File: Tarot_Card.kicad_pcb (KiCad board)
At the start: 2 copper layers, 87 x 64.2 mm, 13 parts, among them U2 ESP32-PICO-D4

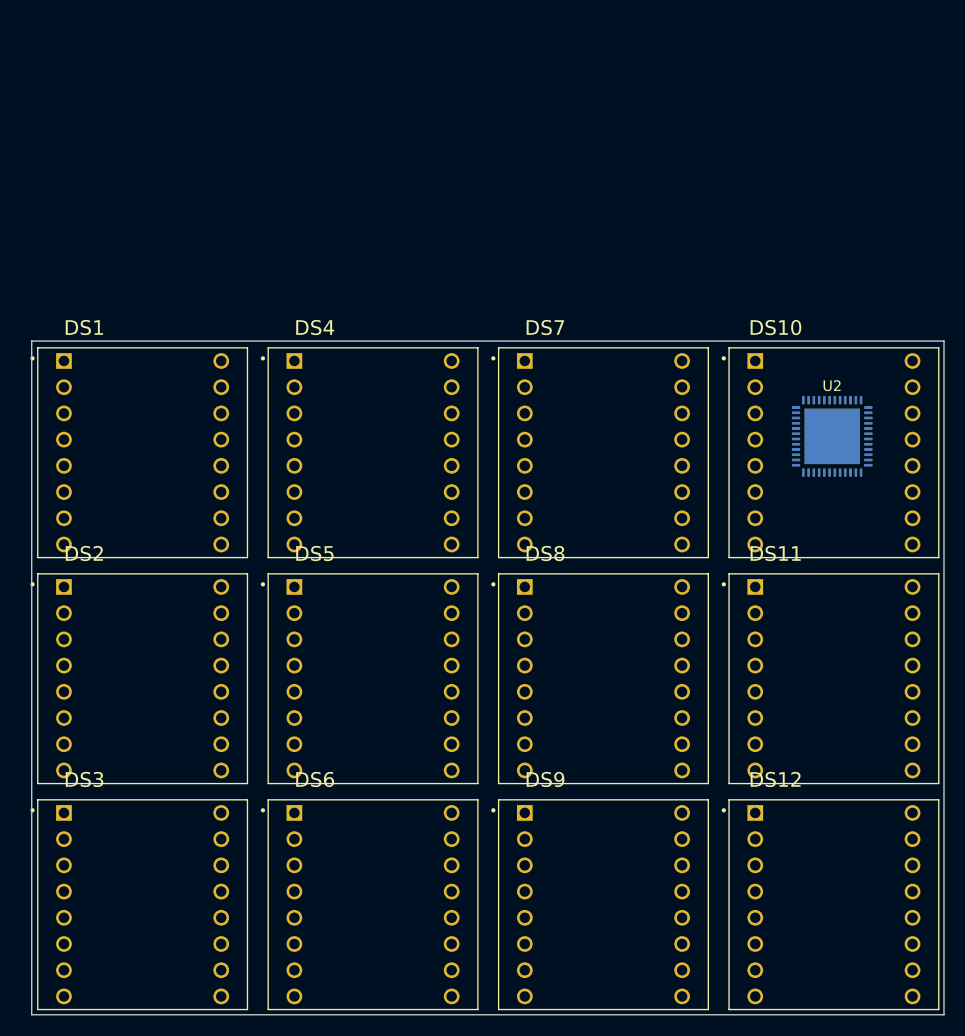
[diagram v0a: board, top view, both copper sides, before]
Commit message: Remove obsolete auto-saved files and backups
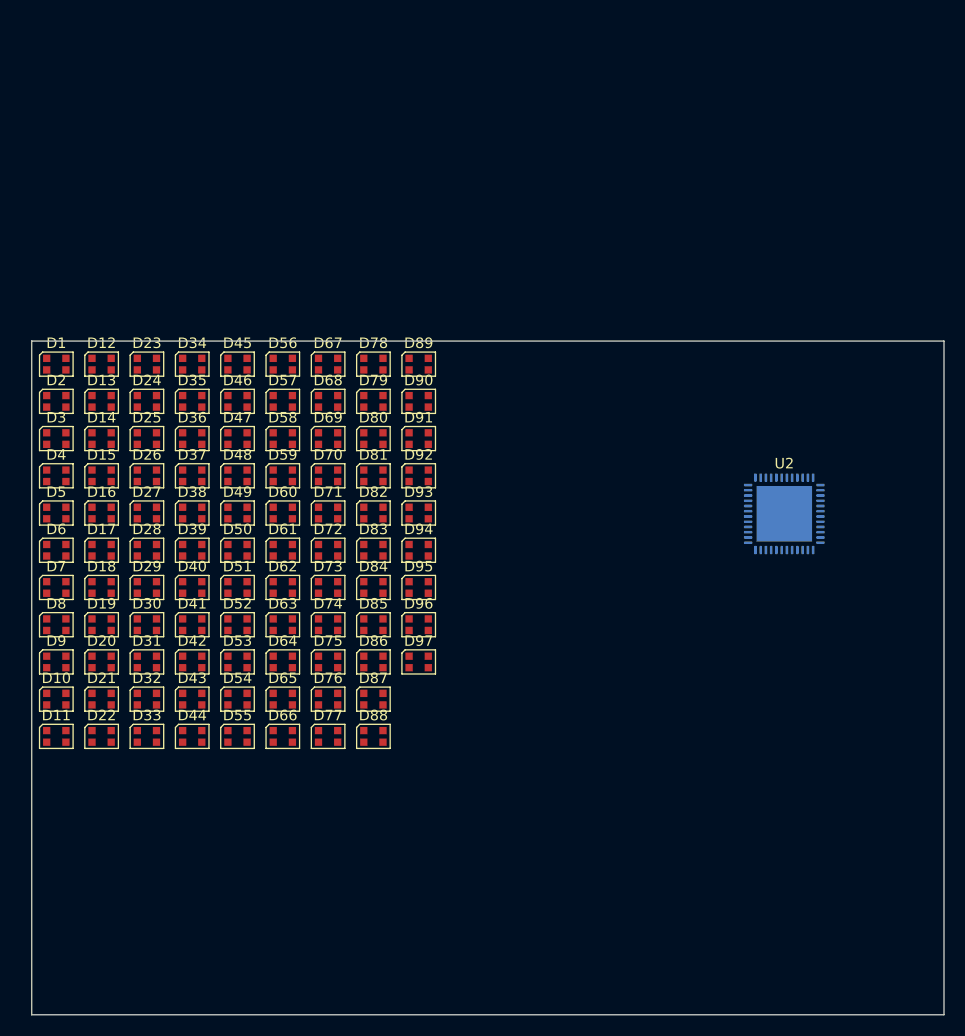
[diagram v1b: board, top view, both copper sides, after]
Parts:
- removed DS1, DS10, DS11, DS12, DS2, DS3, DS4, DS5, DS6, DS7, DS8, DS9: TA08-81GWA, Parts:DISPLAY_TA08-81GWA
- added D1: WS2812B-2020, LED_SMD:LED_WS2812B-2020_PLCC4_2.0x2.0mm, F.Cu at (96.8, 64.0)
- added D10: WS2812B-2020, LED_SMD:LED_WS2812B-2020_PLCC4_2.0x2.0mm, F.Cu at (96.8, 95.9)
- added D11: WS2812B-2020, LED_SMD:LED_WS2812B-2020_PLCC4_2.0x2.0mm, F.Cu at (96.8, 99.5)
- added D12: WS2812B-2020, LED_SMD:LED_WS2812B-2020_PLCC4_2.0x2.0mm, F.Cu at (101.2, 64.0)
- added D13: WS2812B-2020, LED_SMD:LED_WS2812B-2020_PLCC4_2.0x2.0mm, F.Cu at (101.2, 67.5)
- added D14: WS2812B-2020, LED_SMD:LED_WS2812B-2020_PLCC4_2.0x2.0mm, F.Cu at (101.2, 71.0)
- added D15: WS2812B-2020, LED_SMD:LED_WS2812B-2020_PLCC4_2.0x2.0mm, F.Cu at (101.2, 74.6)
- added D16: WS2812B-2020, LED_SMD:LED_WS2812B-2020_PLCC4_2.0x2.0mm, F.Cu at (101.2, 78.2)
- added D17: WS2812B-2020, LED_SMD:LED_WS2812B-2020_PLCC4_2.0x2.0mm, F.Cu at (101.2, 81.7)
- added D18: WS2812B-2020, LED_SMD:LED_WS2812B-2020_PLCC4_2.0x2.0mm, F.Cu at (101.2, 85.2)
- added D19: WS2812B-2020, LED_SMD:LED_WS2812B-2020_PLCC4_2.0x2.0mm, F.Cu at (101.2, 88.8)
- added D2: WS2812B-2020, LED_SMD:LED_WS2812B-2020_PLCC4_2.0x2.0mm, F.Cu at (96.8, 67.5)
- added D20: WS2812B-2020, LED_SMD:LED_WS2812B-2020_PLCC4_2.0x2.0mm, F.Cu at (101.2, 92.3)
- added D21: WS2812B-2020, LED_SMD:LED_WS2812B-2020_PLCC4_2.0x2.0mm, F.Cu at (101.2, 95.9)
- added D22: WS2812B-2020, LED_SMD:LED_WS2812B-2020_PLCC4_2.0x2.0mm, F.Cu at (101.2, 99.5)
- added D23: WS2812B-2020, LED_SMD:LED_WS2812B-2020_PLCC4_2.0x2.0mm, F.Cu at (105.5, 64.0)
- added D24: WS2812B-2020, LED_SMD:LED_WS2812B-2020_PLCC4_2.0x2.0mm, F.Cu at (105.5, 67.5)
- added D25: WS2812B-2020, LED_SMD:LED_WS2812B-2020_PLCC4_2.0x2.0mm, F.Cu at (105.5, 71.0)
- added D26: WS2812B-2020, LED_SMD:LED_WS2812B-2020_PLCC4_2.0x2.0mm, F.Cu at (105.5, 74.6)
- added D27: WS2812B-2020, LED_SMD:LED_WS2812B-2020_PLCC4_2.0x2.0mm, F.Cu at (105.5, 78.2)
- added D28: WS2812B-2020, LED_SMD:LED_WS2812B-2020_PLCC4_2.0x2.0mm, F.Cu at (105.5, 81.7)
- added D29: WS2812B-2020, LED_SMD:LED_WS2812B-2020_PLCC4_2.0x2.0mm, F.Cu at (105.5, 85.2)
- added D3: WS2812B-2020, LED_SMD:LED_WS2812B-2020_PLCC4_2.0x2.0mm, F.Cu at (96.8, 71.0)
- added D30: WS2812B-2020, LED_SMD:LED_WS2812B-2020_PLCC4_2.0x2.0mm, F.Cu at (105.5, 88.8)
- added D31: WS2812B-2020, LED_SMD:LED_WS2812B-2020_PLCC4_2.0x2.0mm, F.Cu at (105.5, 92.3)
- added D32: WS2812B-2020, LED_SMD:LED_WS2812B-2020_PLCC4_2.0x2.0mm, F.Cu at (105.5, 95.9)
- added D33: WS2812B-2020, LED_SMD:LED_WS2812B-2020_PLCC4_2.0x2.0mm, F.Cu at (105.5, 99.5)
- added D34: WS2812B-2020, LED_SMD:LED_WS2812B-2020_PLCC4_2.0x2.0mm, F.Cu at (109.8, 64.0)
- added D35: WS2812B-2020, LED_SMD:LED_WS2812B-2020_PLCC4_2.0x2.0mm, F.Cu at (109.8, 67.5)
- added D36: WS2812B-2020, LED_SMD:LED_WS2812B-2020_PLCC4_2.0x2.0mm, F.Cu at (109.8, 71.0)
- added D37: WS2812B-2020, LED_SMD:LED_WS2812B-2020_PLCC4_2.0x2.0mm, F.Cu at (109.8, 74.6)
- added D38: WS2812B-2020, LED_SMD:LED_WS2812B-2020_PLCC4_2.0x2.0mm, F.Cu at (109.8, 78.2)
- added D39: WS2812B-2020, LED_SMD:LED_WS2812B-2020_PLCC4_2.0x2.0mm, F.Cu at (109.8, 81.7)
- added D4: WS2812B-2020, LED_SMD:LED_WS2812B-2020_PLCC4_2.0x2.0mm, F.Cu at (96.8, 74.6)
- added D40: WS2812B-2020, LED_SMD:LED_WS2812B-2020_PLCC4_2.0x2.0mm, F.Cu at (109.8, 85.2)
- added D41: WS2812B-2020, LED_SMD:LED_WS2812B-2020_PLCC4_2.0x2.0mm, F.Cu at (109.8, 88.8)
- added D42: WS2812B-2020, LED_SMD:LED_WS2812B-2020_PLCC4_2.0x2.0mm, F.Cu at (109.8, 92.3)
- added D43: WS2812B-2020, LED_SMD:LED_WS2812B-2020_PLCC4_2.0x2.0mm, F.Cu at (109.8, 95.9)
- added D44: WS2812B-2020, LED_SMD:LED_WS2812B-2020_PLCC4_2.0x2.0mm, F.Cu at (109.8, 99.5)
- added D45: WS2812B-2020, LED_SMD:LED_WS2812B-2020_PLCC4_2.0x2.0mm, F.Cu at (114.1, 64.0)
- added D46: WS2812B-2020, LED_SMD:LED_WS2812B-2020_PLCC4_2.0x2.0mm, F.Cu at (114.1, 67.5)
- added D47: WS2812B-2020, LED_SMD:LED_WS2812B-2020_PLCC4_2.0x2.0mm, F.Cu at (114.1, 71.0)
- added D48: WS2812B-2020, LED_SMD:LED_WS2812B-2020_PLCC4_2.0x2.0mm, F.Cu at (114.1, 74.6)
- added D49: WS2812B-2020, LED_SMD:LED_WS2812B-2020_PLCC4_2.0x2.0mm, F.Cu at (114.1, 78.2)
- added D5: WS2812B-2020, LED_SMD:LED_WS2812B-2020_PLCC4_2.0x2.0mm, F.Cu at (96.8, 78.2)
- added D50: WS2812B-2020, LED_SMD:LED_WS2812B-2020_PLCC4_2.0x2.0mm, F.Cu at (114.1, 81.7)
- added D51: WS2812B-2020, LED_SMD:LED_WS2812B-2020_PLCC4_2.0x2.0mm, F.Cu at (114.1, 85.2)
- added D52: WS2812B-2020, LED_SMD:LED_WS2812B-2020_PLCC4_2.0x2.0mm, F.Cu at (114.1, 88.8)
- added D53: WS2812B-2020, LED_SMD:LED_WS2812B-2020_PLCC4_2.0x2.0mm, F.Cu at (114.1, 92.3)
- added D54: WS2812B-2020, LED_SMD:LED_WS2812B-2020_PLCC4_2.0x2.0mm, F.Cu at (114.1, 95.9)
- added D55: WS2812B-2020, LED_SMD:LED_WS2812B-2020_PLCC4_2.0x2.0mm, F.Cu at (114.1, 99.5)
- added D56: WS2812B-2020, LED_SMD:LED_WS2812B-2020_PLCC4_2.0x2.0mm, F.Cu at (118.4, 64.0)
- added D57: WS2812B-2020, LED_SMD:LED_WS2812B-2020_PLCC4_2.0x2.0mm, F.Cu at (118.4, 67.5)
- added D58: WS2812B-2020, LED_SMD:LED_WS2812B-2020_PLCC4_2.0x2.0mm, F.Cu at (118.4, 71.0)
- added D59: WS2812B-2020, LED_SMD:LED_WS2812B-2020_PLCC4_2.0x2.0mm, F.Cu at (118.4, 74.6)
- added D6: WS2812B-2020, LED_SMD:LED_WS2812B-2020_PLCC4_2.0x2.0mm, F.Cu at (96.8, 81.7)
- added D60: WS2812B-2020, LED_SMD:LED_WS2812B-2020_PLCC4_2.0x2.0mm, F.Cu at (118.4, 78.2)
- added D61: WS2812B-2020, LED_SMD:LED_WS2812B-2020_PLCC4_2.0x2.0mm, F.Cu at (118.4, 81.7)
- added D62: WS2812B-2020, LED_SMD:LED_WS2812B-2020_PLCC4_2.0x2.0mm, F.Cu at (118.4, 85.2)
- added D63: WS2812B-2020, LED_SMD:LED_WS2812B-2020_PLCC4_2.0x2.0mm, F.Cu at (118.4, 88.8)
- added D64: WS2812B-2020, LED_SMD:LED_WS2812B-2020_PLCC4_2.0x2.0mm, F.Cu at (118.4, 92.3)
- added D65: WS2812B-2020, LED_SMD:LED_WS2812B-2020_PLCC4_2.0x2.0mm, F.Cu at (118.4, 95.9)
- added D66: WS2812B-2020, LED_SMD:LED_WS2812B-2020_PLCC4_2.0x2.0mm, F.Cu at (118.4, 99.5)
- added D67: WS2812B-2020, LED_SMD:LED_WS2812B-2020_PLCC4_2.0x2.0mm, F.Cu at (122.8, 64.0)
- added D68: WS2812B-2020, LED_SMD:LED_WS2812B-2020_PLCC4_2.0x2.0mm, F.Cu at (122.8, 67.5)
- added D69: WS2812B-2020, LED_SMD:LED_WS2812B-2020_PLCC4_2.0x2.0mm, F.Cu at (122.8, 71.0)
- added D7: WS2812B-2020, LED_SMD:LED_WS2812B-2020_PLCC4_2.0x2.0mm, F.Cu at (96.8, 85.2)
- added D70: WS2812B-2020, LED_SMD:LED_WS2812B-2020_PLCC4_2.0x2.0mm, F.Cu at (122.8, 74.6)
- added D71: WS2812B-2020, LED_SMD:LED_WS2812B-2020_PLCC4_2.0x2.0mm, F.Cu at (122.8, 78.2)
- added D72: WS2812B-2020, LED_SMD:LED_WS2812B-2020_PLCC4_2.0x2.0mm, F.Cu at (122.8, 81.7)
- added D73: WS2812B-2020, LED_SMD:LED_WS2812B-2020_PLCC4_2.0x2.0mm, F.Cu at (122.8, 85.2)
- added D74: WS2812B-2020, LED_SMD:LED_WS2812B-2020_PLCC4_2.0x2.0mm, F.Cu at (122.8, 88.8)
- added D75: WS2812B-2020, LED_SMD:LED_WS2812B-2020_PLCC4_2.0x2.0mm, F.Cu at (122.8, 92.3)
- added D76: WS2812B-2020, LED_SMD:LED_WS2812B-2020_PLCC4_2.0x2.0mm, F.Cu at (122.8, 95.9)
- added D77: WS2812B-2020, LED_SMD:LED_WS2812B-2020_PLCC4_2.0x2.0mm, F.Cu at (122.8, 99.5)
- added D78: WS2812B-2020, LED_SMD:LED_WS2812B-2020_PLCC4_2.0x2.0mm, F.Cu at (127.1, 64.0)
- added D79: WS2812B-2020, LED_SMD:LED_WS2812B-2020_PLCC4_2.0x2.0mm, F.Cu at (127.1, 67.5)
- added D8: WS2812B-2020, LED_SMD:LED_WS2812B-2020_PLCC4_2.0x2.0mm, F.Cu at (96.8, 88.8)
- added D80: WS2812B-2020, LED_SMD:LED_WS2812B-2020_PLCC4_2.0x2.0mm, F.Cu at (127.1, 71.0)
- added D81: WS2812B-2020, LED_SMD:LED_WS2812B-2020_PLCC4_2.0x2.0mm, F.Cu at (127.1, 74.6)
- added D82: WS2812B-2020, LED_SMD:LED_WS2812B-2020_PLCC4_2.0x2.0mm, F.Cu at (127.1, 78.2)
- added D83: WS2812B-2020, LED_SMD:LED_WS2812B-2020_PLCC4_2.0x2.0mm, F.Cu at (127.1, 81.7)
- added D84: WS2812B-2020, LED_SMD:LED_WS2812B-2020_PLCC4_2.0x2.0mm, F.Cu at (127.1, 85.2)
- added D85: WS2812B-2020, LED_SMD:LED_WS2812B-2020_PLCC4_2.0x2.0mm, F.Cu at (127.1, 88.8)
- added D86: WS2812B-2020, LED_SMD:LED_WS2812B-2020_PLCC4_2.0x2.0mm, F.Cu at (127.1, 92.3)
- added D87: WS2812B-2020, LED_SMD:LED_WS2812B-2020_PLCC4_2.0x2.0mm, F.Cu at (127.1, 95.9)
- added D88: WS2812B-2020, LED_SMD:LED_WS2812B-2020_PLCC4_2.0x2.0mm, F.Cu at (127.1, 99.5)
- added D89: WS2812B-2020, LED_SMD:LED_WS2812B-2020_PLCC4_2.0x2.0mm, F.Cu at (131.4, 64.0)
- added D9: WS2812B-2020, LED_SMD:LED_WS2812B-2020_PLCC4_2.0x2.0mm, F.Cu at (96.8, 92.3)
- added D90: WS2812B-2020, LED_SMD:LED_WS2812B-2020_PLCC4_2.0x2.0mm, F.Cu at (131.4, 67.5)
- added D91: WS2812B-2020, LED_SMD:LED_WS2812B-2020_PLCC4_2.0x2.0mm, F.Cu at (131.4, 71.0)
- added D92: WS2812B-2020, LED_SMD:LED_WS2812B-2020_PLCC4_2.0x2.0mm, F.Cu at (131.4, 74.6)
- added D93: WS2812B-2020, LED_SMD:LED_WS2812B-2020_PLCC4_2.0x2.0mm, F.Cu at (131.4, 78.2)
- added D94: WS2812B-2020, LED_SMD:LED_WS2812B-2020_PLCC4_2.0x2.0mm, F.Cu at (131.4, 81.7)
- added D95: WS2812B-2020, LED_SMD:LED_WS2812B-2020_PLCC4_2.0x2.0mm, F.Cu at (131.4, 85.2)
- added D96: WS2812B-2020, LED_SMD:LED_WS2812B-2020_PLCC4_2.0x2.0mm, F.Cu at (131.4, 88.8)
- added D97: WS2812B-2020, LED_SMD:LED_WS2812B-2020_PLCC4_2.0x2.0mm, F.Cu at (131.4, 92.3)
- moved U2 8.69 mm to (166.3, 78.2)

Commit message: Remove obsolete backup file; update active layer and BOM export filename in project files
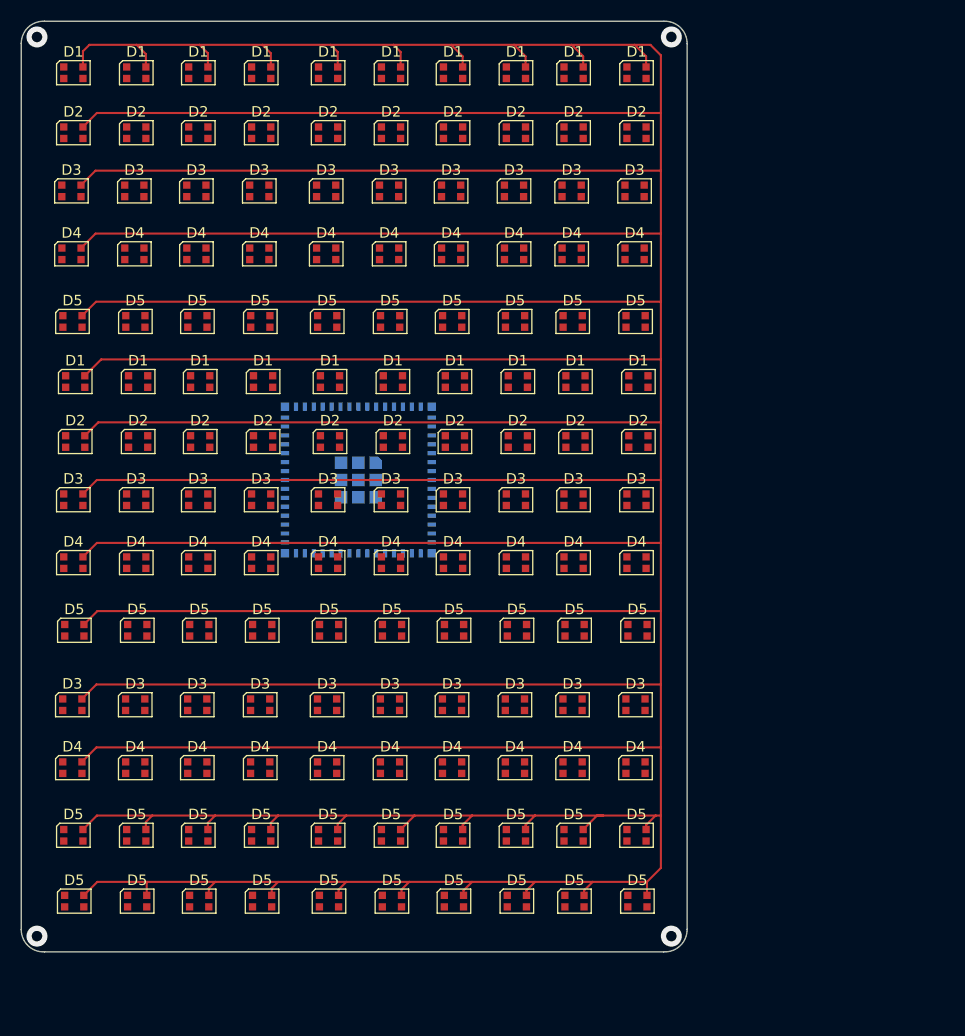
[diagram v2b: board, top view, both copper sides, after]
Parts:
- removed the D1 at (96.8, 64.0)
- removed D10, D11, D12, D13, D14, D15, D16, D17, D18, D19, D20, D21, D22, D23, D24, D25, D26, D27, D28, D29, D30, D31, D32, D33, D34, D35, D36, D37, D38, D39, D40, D41, D42, D43, D44, D45, D46, D47, D48, D49, D50, D51, D52, D53, D54, D55, D56, D57, D58, D59, D6, D60, D61, D62, D63, D64, D65, D66, D67, D68, D69, D7, D70, D71, D72, D73, D74, D75, D76, D77, D78, D79, D8, D80, D81, D82, D83, D84, D85, D86, D87, D88, D89, D9, D90, D91, D92, D93, D94, D95, D96, D97: WS2812B-2020, LED_SMD:LED_WS2812B-2020_PLCC4_2.0x2.0mm
- removed the D2 at (96.8, 67.5)
- removed the D3 at (96.8, 71.0)
- removed the D4 at (96.8, 74.6)
- removed the D5 at (96.8, 78.2)
- removed U2: ESP32-PICO-D4, Package_DFN_QFN:QFN-48-1EP_7x7mm_P0.5mm_EP5.3x5.3mm
- added D1: WS2812B-2020, LED_SMD:LED_WS2812B-2020_PLCC4_2.0x2.0mm, F.Cu at (152.4, 65.6)
- added D1: WS2812B-2020, LED_SMD:LED_WS2812B-2020_PLCC4_2.0x2.0mm, F.Cu at (122.8, 36.2)
- added D1: WS2812B-2020, LED_SMD:LED_WS2812B-2020_PLCC4_2.0x2.0mm, F.Cu at (146.4, 65.6)
- added D1: WS2812B-2020, LED_SMD:LED_WS2812B-2020_PLCC4_2.0x2.0mm, F.Cu at (104.5, 36.2)
- added D1: WS2812B-2020, LED_SMD:LED_WS2812B-2020_PLCC4_2.0x2.0mm, F.Cu at (134.9, 65.6)
- added D1: WS2812B-2020, LED_SMD:LED_WS2812B-2020_PLCC4_2.0x2.0mm, F.Cu at (128.9, 65.6)
- added D1: WS2812B-2020, LED_SMD:LED_WS2812B-2020_PLCC4_2.0x2.0mm, F.Cu at (152.2, 36.2)
- added D1: WS2812B-2020, LED_SMD:LED_WS2812B-2020_PLCC4_2.0x2.0mm, F.Cu at (98.7, 65.6)
- added D1: WS2812B-2020, LED_SMD:LED_WS2812B-2020_PLCC4_2.0x2.0mm, F.Cu at (146.2, 36.2)
- added D1: WS2812B-2020, LED_SMD:LED_WS2812B-2020_PLCC4_2.0x2.0mm, F.Cu at (140.7, 36.2)
- added D1: WS2812B-2020, LED_SMD:LED_WS2812B-2020_PLCC4_2.0x2.0mm, F.Cu at (128.8, 36.2)
- added D1: WS2812B-2020, LED_SMD:LED_WS2812B-2020_PLCC4_2.0x2.0mm, F.Cu at (134.7, 36.2)
- added D1: WS2812B-2020, LED_SMD:LED_WS2812B-2020_PLCC4_2.0x2.0mm, F.Cu at (110.6, 65.6)
- added D1: WS2812B-2020, LED_SMD:LED_WS2812B-2020_PLCC4_2.0x2.0mm, F.Cu at (110.4, 36.2)
- added D1: WS2812B-2020, LED_SMD:LED_WS2812B-2020_PLCC4_2.0x2.0mm, F.Cu at (98.5, 36.2)
- added D1: WS2812B-2020, LED_SMD:LED_WS2812B-2020_PLCC4_2.0x2.0mm, F.Cu at (140.9, 65.6)
- added D1: WS2812B-2020, LED_SMD:LED_WS2812B-2020_PLCC4_2.0x2.0mm, F.Cu at (116.4, 36.2)
- added D1: WS2812B-2020, LED_SMD:LED_WS2812B-2020_PLCC4_2.0x2.0mm, F.Cu at (122.9, 65.6)
- added D1: WS2812B-2020, LED_SMD:LED_WS2812B-2020_PLCC4_2.0x2.0mm, F.Cu at (116.6, 65.6)
- added D1: WS2812B-2020, LED_SMD:LED_WS2812B-2020_PLCC4_2.0x2.0mm, F.Cu at (104.7, 65.6)
- added D2: WS2812B-2020, LED_SMD:LED_WS2812B-2020_PLCC4_2.0x2.0mm, F.Cu at (110.6, 71.3)
- added D2: WS2812B-2020, LED_SMD:LED_WS2812B-2020_PLCC4_2.0x2.0mm, F.Cu at (128.9, 71.3)
- added D2: WS2812B-2020, LED_SMD:LED_WS2812B-2020_PLCC4_2.0x2.0mm, F.Cu at (104.7, 71.3)
- added D2: WS2812B-2020, LED_SMD:LED_WS2812B-2020_PLCC4_2.0x2.0mm, F.Cu at (146.2, 41.9)
- added D2: WS2812B-2020, LED_SMD:LED_WS2812B-2020_PLCC4_2.0x2.0mm, F.Cu at (140.9, 71.3)
- added D2: WS2812B-2020, LED_SMD:LED_WS2812B-2020_PLCC4_2.0x2.0mm, F.Cu at (122.9, 71.3)
- added D2: WS2812B-2020, LED_SMD:LED_WS2812B-2020_PLCC4_2.0x2.0mm, F.Cu at (140.7, 41.9)
- added D2: WS2812B-2020, LED_SMD:LED_WS2812B-2020_PLCC4_2.0x2.0mm, F.Cu at (116.6, 71.3)
- added D2: WS2812B-2020, LED_SMD:LED_WS2812B-2020_PLCC4_2.0x2.0mm, F.Cu at (146.4, 71.3)
- added D2: WS2812B-2020, LED_SMD:LED_WS2812B-2020_PLCC4_2.0x2.0mm, F.Cu at (110.4, 41.9)
- added D2: WS2812B-2020, LED_SMD:LED_WS2812B-2020_PLCC4_2.0x2.0mm, F.Cu at (116.4, 41.9)
- added D2: WS2812B-2020, LED_SMD:LED_WS2812B-2020_PLCC4_2.0x2.0mm, F.Cu at (152.2, 41.9)
- added D2: WS2812B-2020, LED_SMD:LED_WS2812B-2020_PLCC4_2.0x2.0mm, F.Cu at (104.5, 41.9)
- added D2: WS2812B-2020, LED_SMD:LED_WS2812B-2020_PLCC4_2.0x2.0mm, F.Cu at (128.8, 41.9)
- added D2: WS2812B-2020, LED_SMD:LED_WS2812B-2020_PLCC4_2.0x2.0mm, F.Cu at (152.4, 71.3)
- added D2: WS2812B-2020, LED_SMD:LED_WS2812B-2020_PLCC4_2.0x2.0mm, F.Cu at (134.7, 41.9)
- added D2: WS2812B-2020, LED_SMD:LED_WS2812B-2020_PLCC4_2.0x2.0mm, F.Cu at (98.5, 41.9)
- added D2: WS2812B-2020, LED_SMD:LED_WS2812B-2020_PLCC4_2.0x2.0mm, F.Cu at (134.9, 71.3)
- added D2: WS2812B-2020, LED_SMD:LED_WS2812B-2020_PLCC4_2.0x2.0mm, F.Cu at (98.7, 71.3)
- added D2: WS2812B-2020, LED_SMD:LED_WS2812B-2020_PLCC4_2.0x2.0mm, F.Cu at (122.8, 41.9)
- added D3: WS2812B-2020, LED_SMD:LED_WS2812B-2020_PLCC4_2.0x2.0mm, F.Cu at (128.6, 47.4)
- added D3: WS2812B-2020, LED_SMD:LED_WS2812B-2020_PLCC4_2.0x2.0mm, F.Cu at (128.7, 96.4)
- added D3: WS2812B-2020, LED_SMD:LED_WS2812B-2020_PLCC4_2.0x2.0mm, F.Cu at (134.6, 96.4)
- added D3: WS2812B-2020, LED_SMD:LED_WS2812B-2020_PLCC4_2.0x2.0mm, F.Cu at (140.6, 96.4)
- added D3: WS2812B-2020, LED_SMD:LED_WS2812B-2020_PLCC4_2.0x2.0mm, F.Cu at (110.2, 47.4)
- added D3: WS2812B-2020, LED_SMD:LED_WS2812B-2020_PLCC4_2.0x2.0mm, F.Cu at (146.0, 47.4)
- added D3: WS2812B-2020, LED_SMD:LED_WS2812B-2020_PLCC4_2.0x2.0mm, F.Cu at (140.5, 47.4)
- added D3: WS2812B-2020, LED_SMD:LED_WS2812B-2020_PLCC4_2.0x2.0mm, F.Cu at (134.7, 76.9)
- added D3: WS2812B-2020, LED_SMD:LED_WS2812B-2020_PLCC4_2.0x2.0mm, F.Cu at (152.2, 76.9)
- added D3: WS2812B-2020, LED_SMD:LED_WS2812B-2020_PLCC4_2.0x2.0mm, F.Cu at (104.3, 47.4)
- added D3: WS2812B-2020, LED_SMD:LED_WS2812B-2020_PLCC4_2.0x2.0mm, F.Cu at (122.8, 76.9)
- added D3: WS2812B-2020, LED_SMD:LED_WS2812B-2020_PLCC4_2.0x2.0mm, F.Cu at (98.3, 47.4)
- added D3: WS2812B-2020, LED_SMD:LED_WS2812B-2020_PLCC4_2.0x2.0mm, F.Cu at (146.1, 96.4)
- added D3: WS2812B-2020, LED_SMD:LED_WS2812B-2020_PLCC4_2.0x2.0mm, F.Cu at (128.8, 76.9)
- added D3: WS2812B-2020, LED_SMD:LED_WS2812B-2020_PLCC4_2.0x2.0mm, F.Cu at (152.0, 47.4)
- added D3: WS2812B-2020, LED_SMD:LED_WS2812B-2020_PLCC4_2.0x2.0mm, F.Cu at (98.4, 96.4)
- added D3: WS2812B-2020, LED_SMD:LED_WS2812B-2020_PLCC4_2.0x2.0mm, F.Cu at (98.5, 76.9)
- added D3: WS2812B-2020, LED_SMD:LED_WS2812B-2020_PLCC4_2.0x2.0mm, F.Cu at (152.1, 96.4)
- added D3: WS2812B-2020, LED_SMD:LED_WS2812B-2020_PLCC4_2.0x2.0mm, F.Cu at (140.7, 76.9)
- added D3: WS2812B-2020, LED_SMD:LED_WS2812B-2020_PLCC4_2.0x2.0mm, F.Cu at (110.3, 96.4)
- added D3: WS2812B-2020, LED_SMD:LED_WS2812B-2020_PLCC4_2.0x2.0mm, F.Cu at (122.7, 96.4)
- added D3: WS2812B-2020, LED_SMD:LED_WS2812B-2020_PLCC4_2.0x2.0mm, F.Cu at (122.6, 47.4)
- added D3: WS2812B-2020, LED_SMD:LED_WS2812B-2020_PLCC4_2.0x2.0mm, F.Cu at (116.4, 76.9)
- added D3: WS2812B-2020, LED_SMD:LED_WS2812B-2020_PLCC4_2.0x2.0mm, F.Cu at (104.4, 96.4)
- added D3: WS2812B-2020, LED_SMD:LED_WS2812B-2020_PLCC4_2.0x2.0mm, F.Cu at (104.5, 76.9)
- added D3: WS2812B-2020, LED_SMD:LED_WS2812B-2020_PLCC4_2.0x2.0mm, F.Cu at (146.2, 76.9)
- added D3: WS2812B-2020, LED_SMD:LED_WS2812B-2020_PLCC4_2.0x2.0mm, F.Cu at (116.3, 96.4)
- added D3: WS2812B-2020, LED_SMD:LED_WS2812B-2020_PLCC4_2.0x2.0mm, F.Cu at (110.4, 76.9)
- added D3: WS2812B-2020, LED_SMD:LED_WS2812B-2020_PLCC4_2.0x2.0mm, F.Cu at (116.2, 47.4)
- added D3: WS2812B-2020, LED_SMD:LED_WS2812B-2020_PLCC4_2.0x2.0mm, F.Cu at (134.5, 47.4)
- added D4: WS2812B-2020, LED_SMD:LED_WS2812B-2020_PLCC4_2.0x2.0mm, F.Cu at (122.7, 102.4)
- added D4: WS2812B-2020, LED_SMD:LED_WS2812B-2020_PLCC4_2.0x2.0mm, F.Cu at (140.6, 102.4)
- added D4: WS2812B-2020, LED_SMD:LED_WS2812B-2020_PLCC4_2.0x2.0mm, F.Cu at (98.3, 53.4)
- added D4: WS2812B-2020, LED_SMD:LED_WS2812B-2020_PLCC4_2.0x2.0mm, F.Cu at (122.8, 82.9)
- added D4: WS2812B-2020, LED_SMD:LED_WS2812B-2020_PLCC4_2.0x2.0mm, F.Cu at (152.1, 102.4)
- added D4: WS2812B-2020, LED_SMD:LED_WS2812B-2020_PLCC4_2.0x2.0mm, F.Cu at (134.5, 53.4)
- added D4: WS2812B-2020, LED_SMD:LED_WS2812B-2020_PLCC4_2.0x2.0mm, F.Cu at (134.6, 102.4)
- added D4: WS2812B-2020, LED_SMD:LED_WS2812B-2020_PLCC4_2.0x2.0mm, F.Cu at (128.8, 82.9)
- added D4: WS2812B-2020, LED_SMD:LED_WS2812B-2020_PLCC4_2.0x2.0mm, F.Cu at (128.6, 53.4)
- added D4: WS2812B-2020, LED_SMD:LED_WS2812B-2020_PLCC4_2.0x2.0mm, F.Cu at (104.3, 53.4)
- added D4: WS2812B-2020, LED_SMD:LED_WS2812B-2020_PLCC4_2.0x2.0mm, F.Cu at (116.3, 102.4)
- added D4: WS2812B-2020, LED_SMD:LED_WS2812B-2020_PLCC4_2.0x2.0mm, F.Cu at (146.1, 102.4)
- added D4: WS2812B-2020, LED_SMD:LED_WS2812B-2020_PLCC4_2.0x2.0mm, F.Cu at (146.0, 53.4)
- added D4: WS2812B-2020, LED_SMD:LED_WS2812B-2020_PLCC4_2.0x2.0mm, F.Cu at (110.3, 102.4)
- added D4: WS2812B-2020, LED_SMD:LED_WS2812B-2020_PLCC4_2.0x2.0mm, F.Cu at (152.2, 82.9)
- added D4: WS2812B-2020, LED_SMD:LED_WS2812B-2020_PLCC4_2.0x2.0mm, F.Cu at (110.2, 53.4)
- added D4: WS2812B-2020, LED_SMD:LED_WS2812B-2020_PLCC4_2.0x2.0mm, F.Cu at (110.4, 82.9)
- added D4: WS2812B-2020, LED_SMD:LED_WS2812B-2020_PLCC4_2.0x2.0mm, F.Cu at (122.6, 53.4)
- added D4: WS2812B-2020, LED_SMD:LED_WS2812B-2020_PLCC4_2.0x2.0mm, F.Cu at (116.2, 53.4)
- added D4: WS2812B-2020, LED_SMD:LED_WS2812B-2020_PLCC4_2.0x2.0mm, F.Cu at (140.5, 53.4)
- added D4: WS2812B-2020, LED_SMD:LED_WS2812B-2020_PLCC4_2.0x2.0mm, F.Cu at (134.7, 82.9)
- added D4: WS2812B-2020, LED_SMD:LED_WS2812B-2020_PLCC4_2.0x2.0mm, F.Cu at (98.5, 82.9)
- added D4: WS2812B-2020, LED_SMD:LED_WS2812B-2020_PLCC4_2.0x2.0mm, F.Cu at (98.4, 102.4)
- added D4: WS2812B-2020, LED_SMD:LED_WS2812B-2020_PLCC4_2.0x2.0mm, F.Cu at (140.7, 82.9)
- added D4: WS2812B-2020, LED_SMD:LED_WS2812B-2020_PLCC4_2.0x2.0mm, F.Cu at (104.4, 102.4)
- added D4: WS2812B-2020, LED_SMD:LED_WS2812B-2020_PLCC4_2.0x2.0mm, F.Cu at (152.0, 53.4)
- added D4: WS2812B-2020, LED_SMD:LED_WS2812B-2020_PLCC4_2.0x2.0mm, F.Cu at (104.5, 82.9)
- added D4: WS2812B-2020, LED_SMD:LED_WS2812B-2020_PLCC4_2.0x2.0mm, F.Cu at (128.7, 102.4)
- added D4: WS2812B-2020, LED_SMD:LED_WS2812B-2020_PLCC4_2.0x2.0mm, F.Cu at (116.4, 82.9)
- added D4: WS2812B-2020, LED_SMD:LED_WS2812B-2020_PLCC4_2.0x2.0mm, F.Cu at (146.2, 82.9)
- added D5: WS2812B-2020, LED_SMD:LED_WS2812B-2020_PLCC4_2.0x2.0mm, F.Cu at (134.8, 89.3)
- added D5: WS2812B-2020, LED_SMD:LED_WS2812B-2020_PLCC4_2.0x2.0mm, F.Cu at (128.7, 59.9)
- added D5: WS2812B-2020, LED_SMD:LED_WS2812B-2020_PLCC4_2.0x2.0mm, F.Cu at (128.8, 108.9)
- added D5: WS2812B-2020, LED_SMD:LED_WS2812B-2020_PLCC4_2.0x2.0mm, F.Cu at (140.8, 89.3)
- added D5: WS2812B-2020, LED_SMD:LED_WS2812B-2020_PLCC4_2.0x2.0mm, F.Cu at (152.1, 59.9)
- added D5: WS2812B-2020, LED_SMD:LED_WS2812B-2020_PLCC4_2.0x2.0mm, F.Cu at (104.5, 108.9)
- added D5: WS2812B-2020, LED_SMD:LED_WS2812B-2020_PLCC4_2.0x2.0mm, F.Cu at (116.5, 115.2)
- added D5: WS2812B-2020, LED_SMD:LED_WS2812B-2020_PLCC4_2.0x2.0mm, F.Cu at (146.1, 59.9)
- added D5: WS2812B-2020, LED_SMD:LED_WS2812B-2020_PLCC4_2.0x2.0mm, F.Cu at (152.3, 89.3)
- added D5: WS2812B-2020, LED_SMD:LED_WS2812B-2020_PLCC4_2.0x2.0mm, F.Cu at (110.5, 115.2)
- added D5: WS2812B-2020, LED_SMD:LED_WS2812B-2020_PLCC4_2.0x2.0mm, F.Cu at (98.6, 115.2)
- added D5: WS2812B-2020, LED_SMD:LED_WS2812B-2020_PLCC4_2.0x2.0mm, F.Cu at (134.6, 59.9)
- added D5: WS2812B-2020, LED_SMD:LED_WS2812B-2020_PLCC4_2.0x2.0mm, F.Cu at (122.8, 115.2)
- added D5: WS2812B-2020, LED_SMD:LED_WS2812B-2020_PLCC4_2.0x2.0mm, F.Cu at (134.8, 115.2)
- added D5: WS2812B-2020, LED_SMD:LED_WS2812B-2020_PLCC4_2.0x2.0mm, F.Cu at (140.8, 115.2)
- added D5: WS2812B-2020, LED_SMD:LED_WS2812B-2020_PLCC4_2.0x2.0mm, F.Cu at (122.7, 59.9)
- added D5: WS2812B-2020, LED_SMD:LED_WS2812B-2020_PLCC4_2.0x2.0mm, F.Cu at (116.3, 59.9)
- added D5: WS2812B-2020, LED_SMD:LED_WS2812B-2020_PLCC4_2.0x2.0mm, F.Cu at (152.3, 115.2)
- added D5: WS2812B-2020, LED_SMD:LED_WS2812B-2020_PLCC4_2.0x2.0mm, F.Cu at (134.7, 108.9)
- added D5: WS2812B-2020, LED_SMD:LED_WS2812B-2020_PLCC4_2.0x2.0mm, F.Cu at (128.8, 115.2)
- added D5: WS2812B-2020, LED_SMD:LED_WS2812B-2020_PLCC4_2.0x2.0mm, F.Cu at (110.4, 108.9)
- added D5: WS2812B-2020, LED_SMD:LED_WS2812B-2020_PLCC4_2.0x2.0mm, F.Cu at (152.2, 108.9)
- added D5: WS2812B-2020, LED_SMD:LED_WS2812B-2020_PLCC4_2.0x2.0mm, F.Cu at (98.5, 108.9)
- added D5: WS2812B-2020, LED_SMD:LED_WS2812B-2020_PLCC4_2.0x2.0mm, F.Cu at (104.4, 59.9)
- added D5: WS2812B-2020, LED_SMD:LED_WS2812B-2020_PLCC4_2.0x2.0mm, F.Cu at (116.5, 89.3)
- added D5: WS2812B-2020, LED_SMD:LED_WS2812B-2020_PLCC4_2.0x2.0mm, F.Cu at (110.5, 89.3)
- added D5: WS2812B-2020, LED_SMD:LED_WS2812B-2020_PLCC4_2.0x2.0mm, F.Cu at (116.4, 108.9)
- added D5: WS2812B-2020, LED_SMD:LED_WS2812B-2020_PLCC4_2.0x2.0mm, F.Cu at (122.8, 108.9)
- added D5: WS2812B-2020, LED_SMD:LED_WS2812B-2020_PLCC4_2.0x2.0mm, F.Cu at (140.7, 108.9)
- added D5: WS2812B-2020, LED_SMD:LED_WS2812B-2020_PLCC4_2.0x2.0mm, F.Cu at (128.9, 89.3)
- added D5: WS2812B-2020, LED_SMD:LED_WS2812B-2020_PLCC4_2.0x2.0mm, F.Cu at (146.2, 108.9)
- added D5: WS2812B-2020, LED_SMD:LED_WS2812B-2020_PLCC4_2.0x2.0mm, F.Cu at (98.4, 59.9)
- added D5: WS2812B-2020, LED_SMD:LED_WS2812B-2020_PLCC4_2.0x2.0mm, F.Cu at (104.6, 89.3)
- added D5: WS2812B-2020, LED_SMD:LED_WS2812B-2020_PLCC4_2.0x2.0mm, F.Cu at (98.6, 89.3)
- added D5: WS2812B-2020, LED_SMD:LED_WS2812B-2020_PLCC4_2.0x2.0mm, F.Cu at (110.3, 59.9)
- added D5: WS2812B-2020, LED_SMD:LED_WS2812B-2020_PLCC4_2.0x2.0mm, F.Cu at (104.6, 115.2)
- added D5: WS2812B-2020, LED_SMD:LED_WS2812B-2020_PLCC4_2.0x2.0mm, F.Cu at (140.6, 59.9)
- added D5: WS2812B-2020, LED_SMD:LED_WS2812B-2020_PLCC4_2.0x2.0mm, F.Cu at (146.3, 115.2)
- added D5: WS2812B-2020, LED_SMD:LED_WS2812B-2020_PLCC4_2.0x2.0mm, F.Cu at (122.9, 89.3)
- added D5: WS2812B-2020, LED_SMD:LED_WS2812B-2020_PLCC4_2.0x2.0mm, F.Cu at (146.3, 89.3)
- added U1: ESP32-S3-MINI-1U, RF_Module:ESP32-S2-MINI-1U, B.Cu at (125.7, 75.0)
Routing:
- net VDD: track 0.00 -> 911.3 mm
- net /DIN: vias 0 -> 1
- net (no net): vias 0 -> 3
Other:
- board size 87 x 64.2 mm -> 63.5 x 88.8 mm
